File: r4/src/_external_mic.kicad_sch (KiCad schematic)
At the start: 138 parts, among them J27 , Q12 BSS84PW, Q13 BSS84PW, Q14 NX6008NBKW, Q15 NX3008NBKW, Q16 NX3008NBKW, Q17 NX3008NBKW, Q18 NX3008NBKW, Q19 NX3008NBKW, Q20 BSS84PW, Q21 BSS84PW, Q22 NX3008NBKW, Q23 NX3008NBKW, Q24 NX3008NBKW, Q25 BSS84PW, T17 , T18 , T19 , T20 , T21 , T22 , T23 , T24 , T25 , T26 , T27 , T28 , T29 , T30 , T31 , T32 , T33 , T34 , T35 , T36 , T37 , T38 , T43 , T44 , T45 , T46 , T47 , T48 , T49 , T50 , U17 74HC20, U18 THAT5173, U19 74HC74, U20 74HC132, U21 74HC4520, U22 74HC132, U23 THAT1580, U24 74HC688, U25 LM4562, U26 74HC688, U27 AD4005

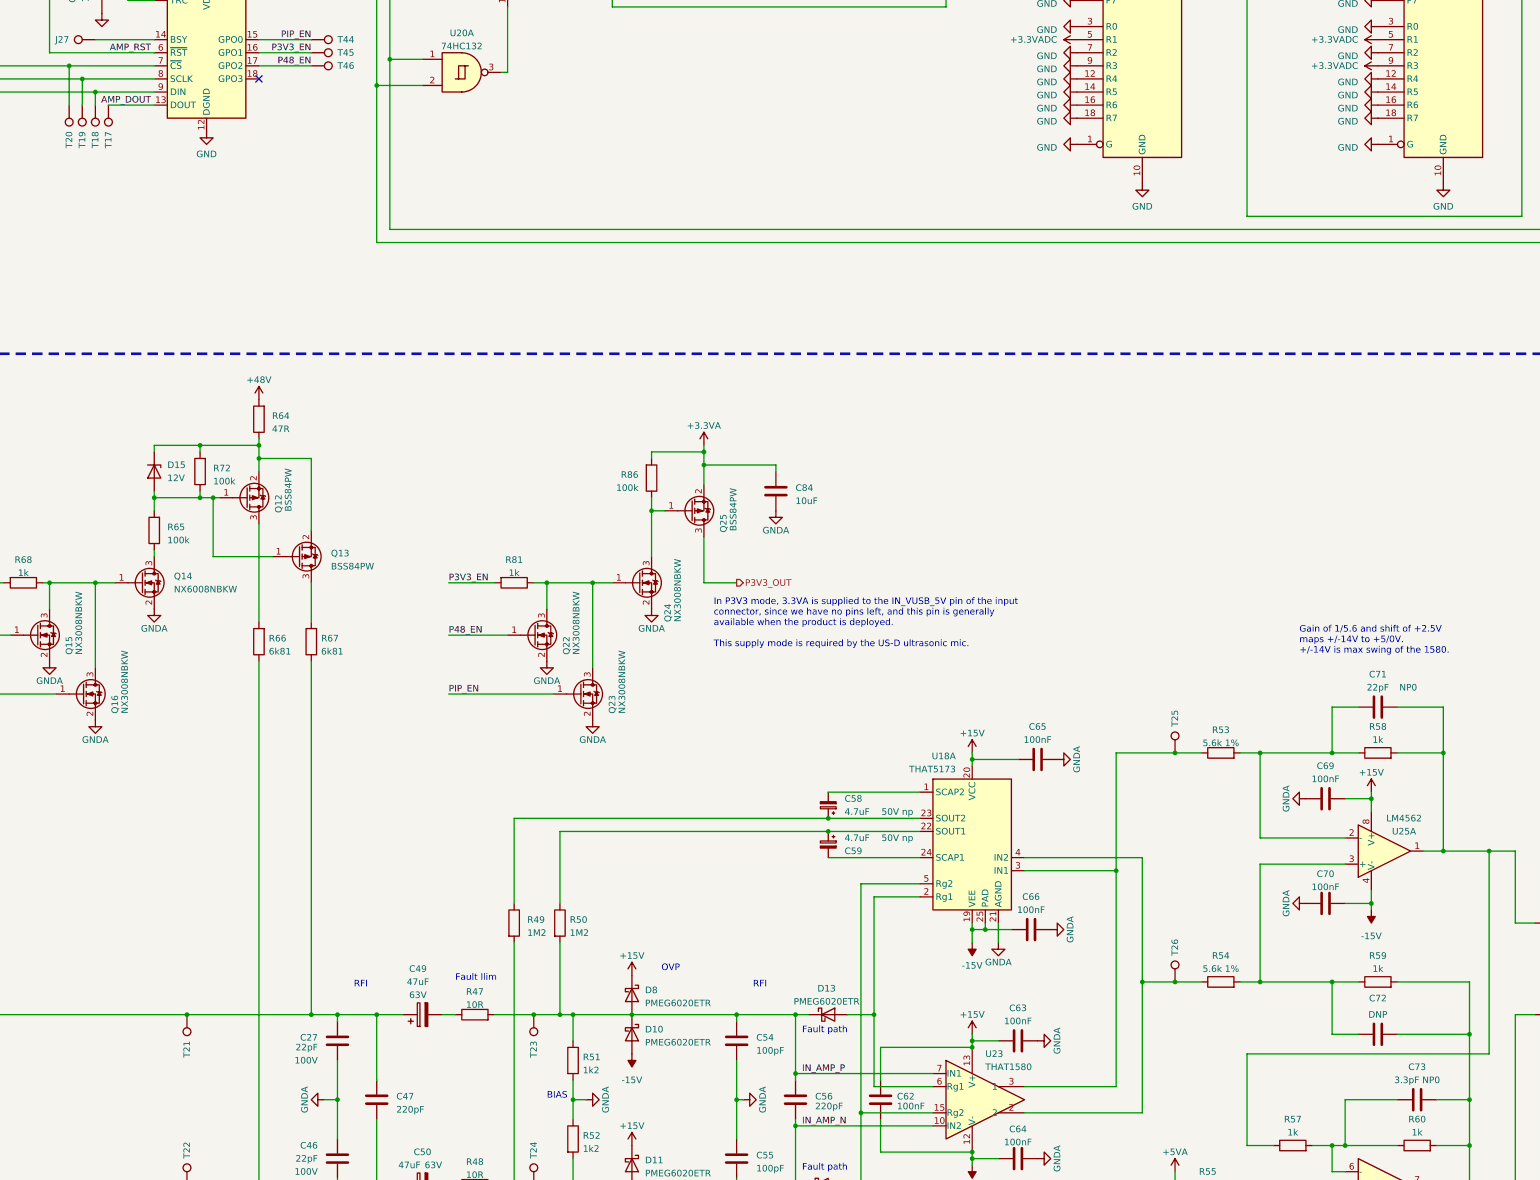
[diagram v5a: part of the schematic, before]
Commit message: Set volage ratings on some caps, change some cap footprints to remove a couple of BOM lines
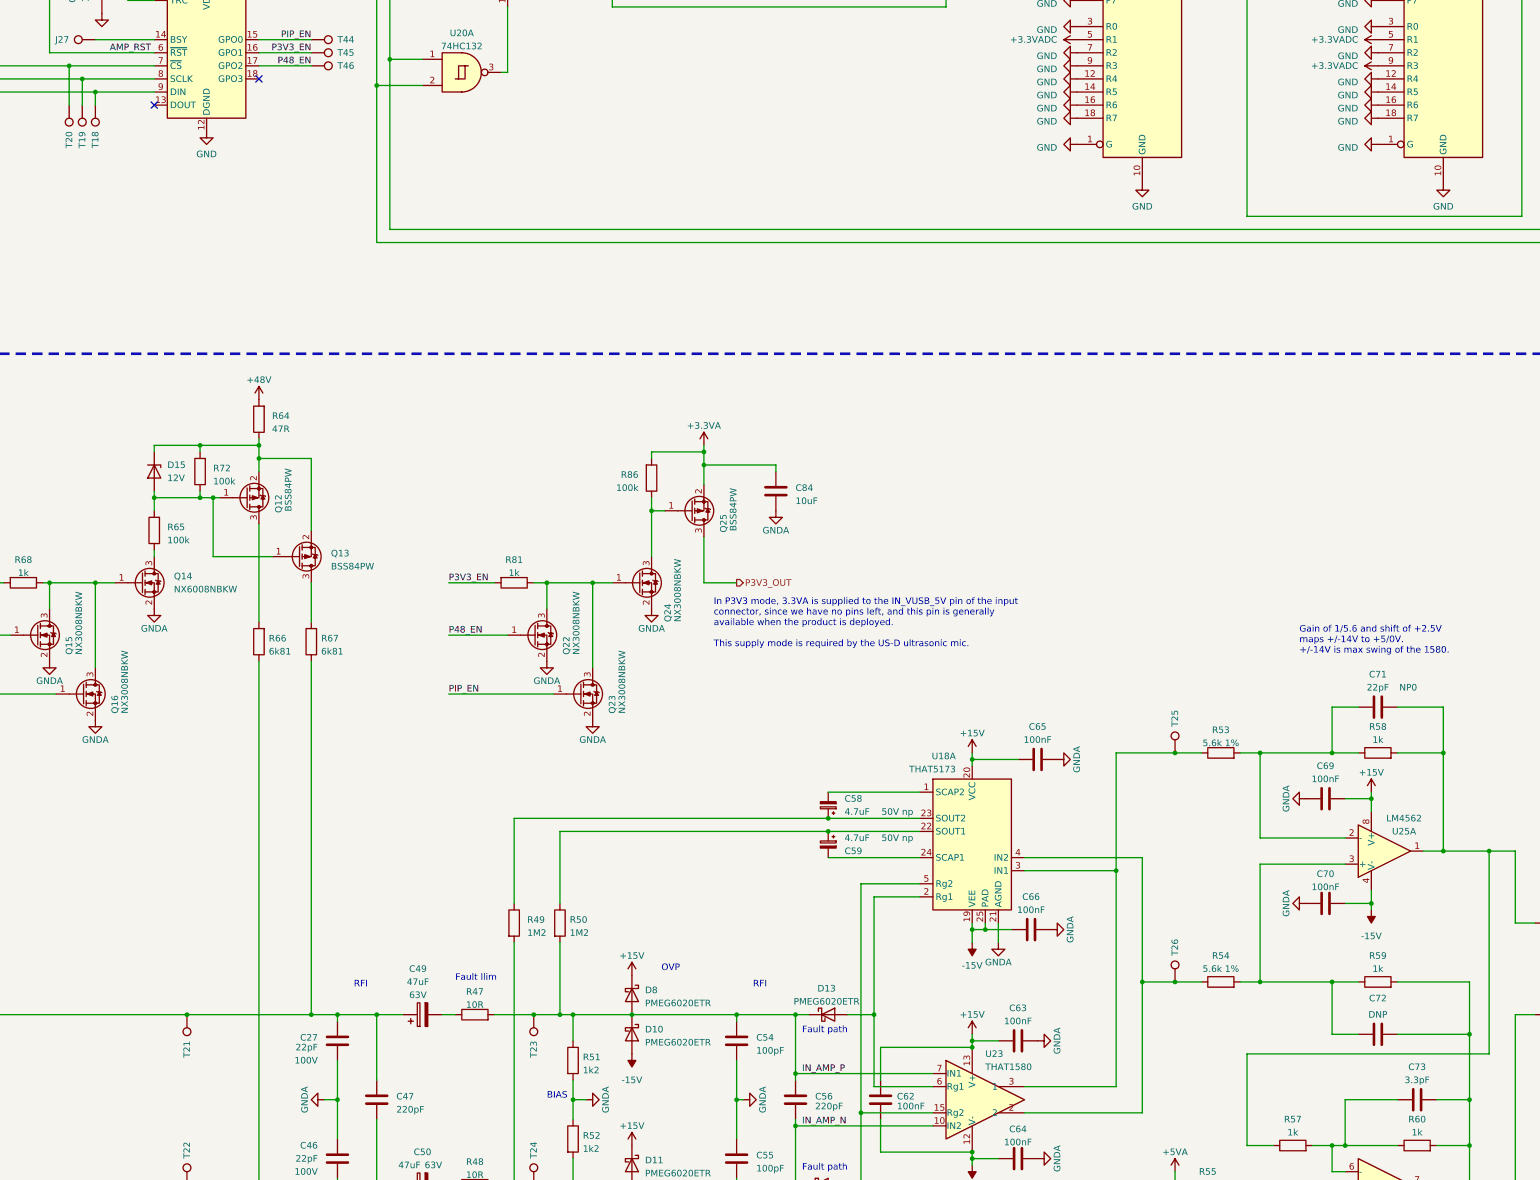
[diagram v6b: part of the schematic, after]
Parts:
- removed T17: (no value), TestPoint:TestPoint_Pad_D1.0mm, symbol Connector:TestPoint
- C56: footprint Capacitor_SMD:C_0201_0603Metric -> Capacitor_SMD:C_0402_1005Metric
- C73: value 3.3pF NP0 -> 3.3pF; Tempco (none) -> NP0
- C77: footprint Capacitor_SMD:C_0805_2012Metric -> Capacitor_SMD:C_0603_1608Metric; Voltage (none) -> 6.3V
- C83, C84: Voltage (none) -> 6.3V
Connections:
- net AMP_DOUT: no longer names the net of U18.13 (DOUT)
- no-connect marks 8 -> 9
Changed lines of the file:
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@@
   (no_connect (at 257.81 118.11))
   (no_connect (at 210.82 31.75))
+  (no_connect (at 181.61 142.24))
   (wire (pts (xy 417.83 276.86) (xy 417.83 275.59))
     (stroke (width 0) (type default))
@@
     (stroke (width 0) (type default))
   )
-  (wire (pts (xy 172.72 142.24) (xy 181.61 142.24))
-    (stroke (width 0) (type default))
-  )
   (wire (pts (xy 482.6 152.4) (xy 482.6 143.51))
     (stroke (width 0) (type default))
@@
     (effects (font (size 1.27 1.27)) (justify left bottom))
   )
-  (label "AMP_DOUT" (at 180.975 142.24 180) (fields_autoplaced)
-    (effects (font (size 1.27 1.27)) (justify right bottom))
-  )
   (label "IN_AMP_P" (at 307.34 330.2 0) (fields_autoplaced)
     (effects (font (size 1.27 1.27)) (justify left bottom))
@@
       (effects (font (size 1.27 1.27)))
     )
-    (property "Value" "3.3pF NP0" (at 426.72 331.47 90)
+    (property "Value" "3.3pF" (at 426.72 331.47 90)
       (effects (font (size 1.27 1.27)))
     )
@@
       (effects (font (size 1.27 1.27)) hide)
     )
+    (property "Tempco" "NP0" (at 426.72 335.28 90)
+      (effects (font (size 1.27 1.27)) hide)
+    )
     (pin "1")
     (pin "2")
@@
       (project "bugg-main-r4"
         (path "/e3eb514f-6ce4-4abe-ba20-f82f0015628f/41f15edd-4583-4f5d-8a81-daeb7c83b416"
-          (reference "C73") (unit 1) (value "3.3pF NP0") (footprint "Capacitor_SMD:C_0402_1005Metric")
+          (reference "C73") (unit 1) (value "3.3pF") (footprint "Capacitor_SMD:C_0402_1005Metric")
         )
       )
@@
       (effects (font (size 1.27 1.27)) hide)
     )
+    (property "Voltage" "6.3V" (at 302.26 217.17 0)
+      (effects (font (size 1.27 1.27)) hide)
+    )
     (pin "1")
     (pin "2")
@@
       (effects (font (size 1.27 1.27)) hide)
     )
+    (property "Voltage" "6.3V" (at 132.08 217.17 0)
+      (effects (font (size 1.27 1.27)) hide)
+    )
     (pin "1")
     (pin "2")
@@
       (effects (font (size 1.27 1.27)) (justify right))
     )
-    (property "Footprint" "Capacitor_SMD:C_0201_0603Metric" (at 305.1048 331.47 0)
+    (property "Footprint" "Capacitor_SMD:C_0402_1005Metric" (at 305.1048 331.47 0)
       (effects (font (size 1.27 1.27)) hide)
     )
@@
       (project "bugg-main-r4"
         (path "/e3eb514f-6ce4-4abe-ba20-f82f0015628f/41f15edd-4583-4f5d-8a81-daeb7c83b416"
-          (reference "C56") (unit 1) (value "220pF") (footprint "Capacitor_SMD:C_0201_0603Metric")
+          (reference "C56") (unit 1) (value "220pF") (footprint "Capacitor_SMD:C_0402_1005Metric")
         )
       )
@@
     )
   )
-  (symbol (lib_id "Connector:TestPoint") (at 172.72 142.24 180) (unit 1)
-    (in_bom yes) (on_board yes) (dnp no)
-    (property "Reference" "T17" (at 172.72 147.32 90)
-      (effects (font (size 1.27 1.27)) (justify left))
-    )
-    (property "Value" " " (at 171.45 147.32 90)
-      (effects (font (size 1.27 1.27)) (justify left))
-    )
-    (property "Footprint" "TestPoint:TestPoint_Pad_D1.0mm" (at 167.64 142.24 0)
-      (effects (font (size 1.27 1.27)) hide)
-    )
-    (property "Datasheet" "~" (at 167.64 142.24 0)
-      (effects (font (size 1.27 1.27)) hide)
-    )
-    (pin "1")
-    (instances
-      (project "bugg-main-r4"
-        (path "/e3eb514f-6ce4-4abe-ba20-f82f0015628f/41f15edd-4583-4f5d-8a81-daeb7c83b416"
-          (reference "T17") (unit 1) (value " ") (footprint "TestPoint:TestPoint_Pad_D1.0mm")
-        )
-      )
-    )
-  )
   (symbol (lib_id "Device:R") (at 76.2 234.95 270) (unit 1)
     (in_bom yes) (on_board yes) (dnp no) (fields_autoplaced)
@@
       (effects (font (size 1.27 1.27)))
     )
-    (property "Footprint" "Capacitor_SMD:C_0805_2012Metric" (at 474.98 276.5552 0)
+    (property "Footprint" "Capacitor_SMD:C_0603_1608Metric" (at 474.98 276.5552 0)
       (effects (font (size 1.27 1.27)) hide)
     )
@@
       (effects (font (size 1.27 1.27)) hide)
     )
+    (property "Voltage" "6.3V" (at 478.79 275.59 90)
+      (effects (font (size 1.27 1.27)) hide)
+    )
     (pin "1")
     (pin "2")
@@
       (project "bugg-main-r4"
         (path "/e3eb514f-6ce4-4abe-ba20-f82f0015628f/41f15edd-4583-4f5d-8a81-daeb7c83b416"
-          (reference "C77") (unit 1) (value "10uF") (footprint "Capacitor_SMD:C_0805_2012Metric")
+          (reference "C77") (unit 1) (value "10uF") (footprint "Capacitor_SMD:C_0603_1608Metric")
         )
       )

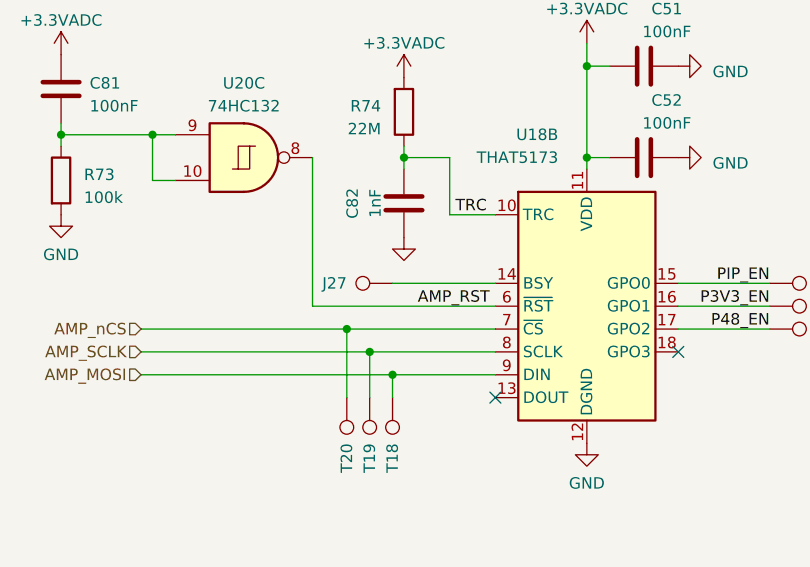
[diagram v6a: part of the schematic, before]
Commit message: Remove unnecessary BSY testpoint
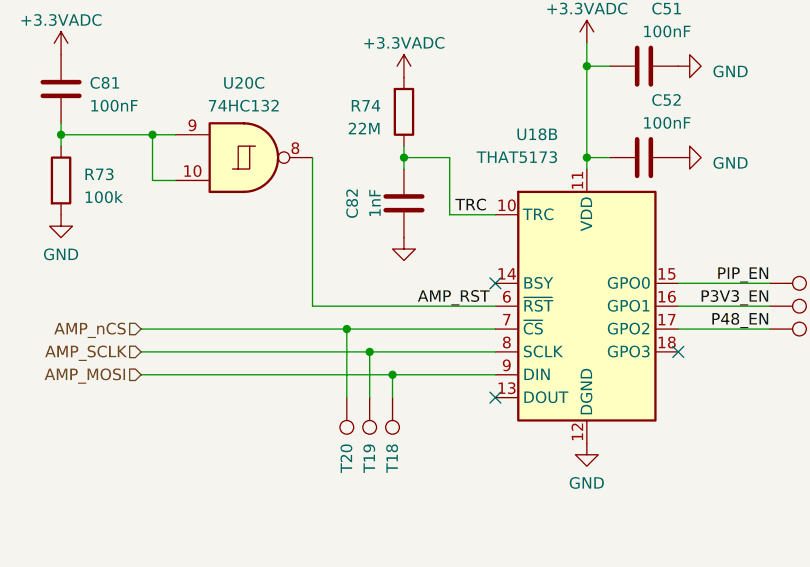
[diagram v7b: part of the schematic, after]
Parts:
- removed J27: (no value), TestPoint:TestPoint_Pad_D1.0mm, symbol Connector:TestPoint
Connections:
- no-connect marks 9 -> 10
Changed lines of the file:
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@@
   (no_connect (at 509.27 119.38))
   (no_connect (at 201.93 137.16))
+  (no_connect (at 181.61 129.54))
   (no_connect (at 257.81 118.11))
   (no_connect (at 210.82 31.75))
@@
     (stroke (width 0) (type default))
   )
-  (wire (pts (xy 181.61 129.54) (xy 170.18 129.54))
-    (stroke (width 0) (type default))
-  )
   (wire (pts (xy 472.44 275.59) (xy 472.44 289.56))
     (stroke (width 0) (type default))
@@
         )
       )
-    )
-  )
-  (symbol (lib_id "Connector:TestPoint") (at 170.18 129.54 90) (unit 1)
-    (in_bom yes) (on_board yes) (dnp no)
-    (property "Reference" "J27" (at 165.1 129.54 90)
-      (effects (font (size 1.27 1.27)) (justify left))
-    )
-    (property "Value" " " (at 165.1 128.27 90)
-      (effects (font (size 1.27 1.27)) (justify left))
-    )
-    (property "Footprint" "TestPoint:TestPoint_Pad_D1.0mm" (at 170.18 124.46 0)
-      (effects (font (size 1.27 1.27)) hide)
-    )
-    (property "Datasheet" "~" (at 170.18 124.46 0)
-      (effects (font (size 1.27 1.27)) hide)
-    )
-    (pin "1")
-    (instances
-      (project "bugg-main-r4"
-        (path "/e3eb514f-6ce4-4abe-ba20-f82f0015628f/41f15edd-4583-4f5d-8a81-daeb7c83b416"
-          (reference "J27") (unit 1) (value " ") (footprint "TestPoint:TestPoint_Pad_D1.0mm")
-        )
-      )

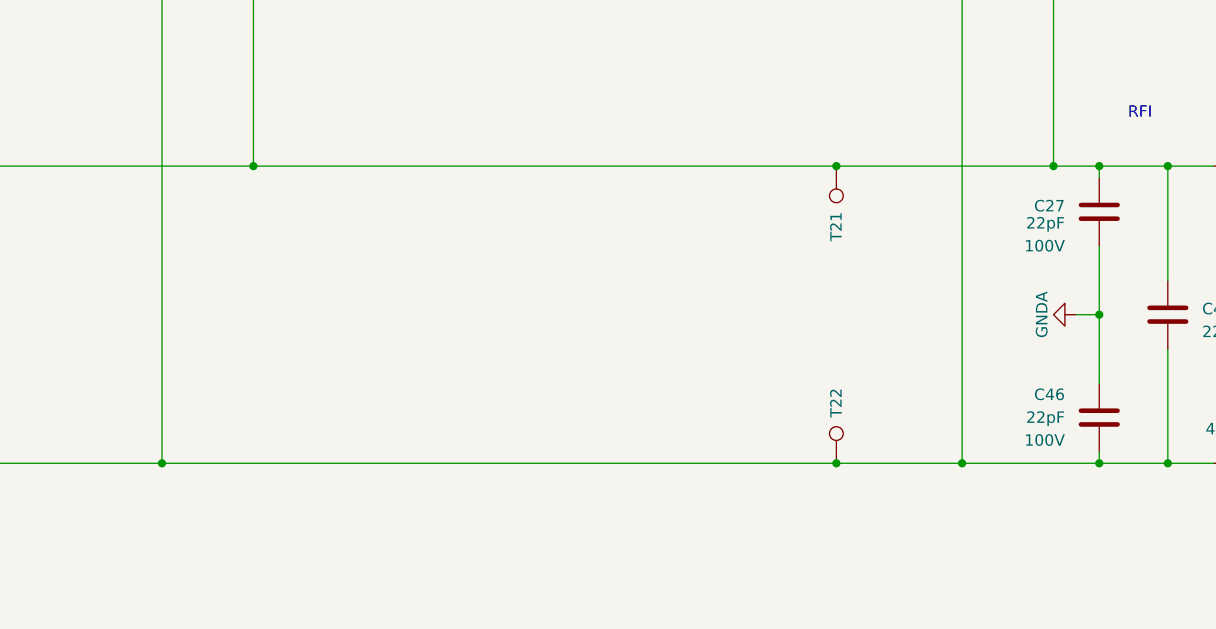
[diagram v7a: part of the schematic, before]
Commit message: Remove testpoints from mic inputs - there's no space for them
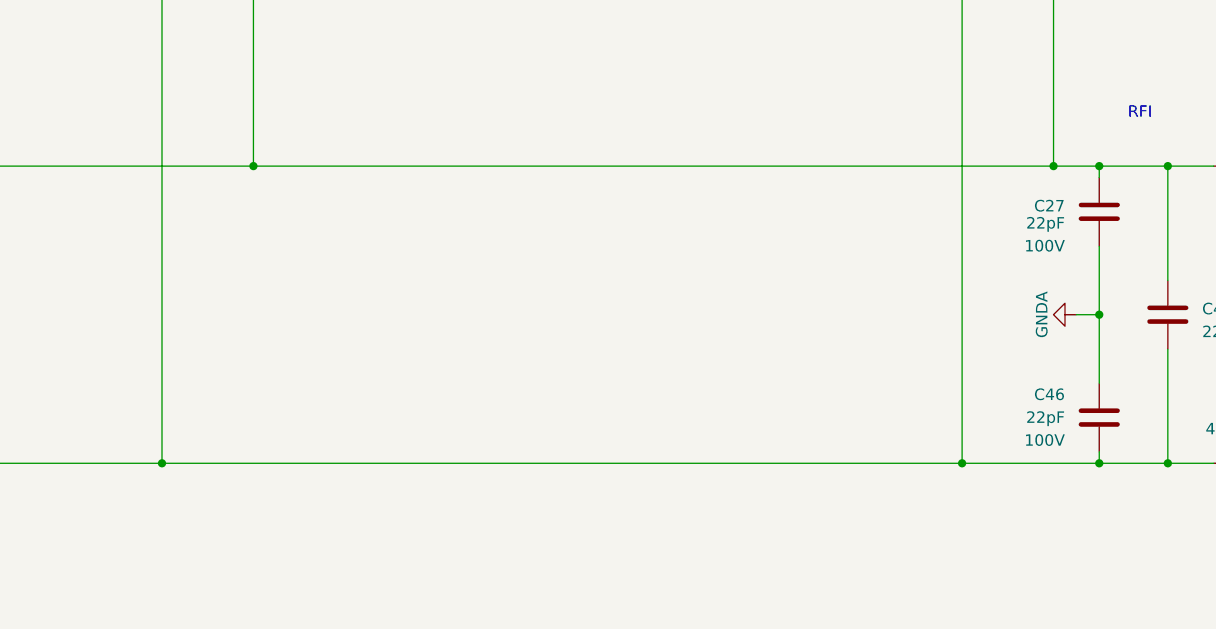
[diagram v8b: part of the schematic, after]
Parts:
- removed T21, T22: (no value), TestPoint:TestPoint_Pad_D1.0mm, symbol Connector:TestPoint
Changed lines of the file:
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@@
   (junction (at 340.36 302.26) (diameter 0) (color 0 0 0 0)
   )
-  (junction (at 187.96 318.77) (diameter 0) (color 0 0 0 0)
-  )
   (junction (at 262.89 351.79) (diameter 0) (color 0 0 0 0)
   )
@@
   (junction (at 528.32 143.51) (diameter 0) (color 0 0 0 0)
   )
-  (junction (at 187.96 351.79) (diameter 0) (color 0 0 0 0)
-  )
   (junction (at 306.07 82.55) (diameter 0) (color 0 0 0 0)
   )
@@
     (stroke (width 0) (type default))
   )
-  (wire (pts (xy 187.96 351.79) (xy 201.93 351.79))
+  (wire (pts (xy 113.03 351.79) (xy 201.93 351.79))
     (stroke (width 0) (type default))
   )
@@
     (stroke (width 0) (type default))
   )
-  (wire (pts (xy 123.19 318.77) (xy 187.96 318.77))
-    (stroke (width 0) (type default))
-  )
   (wire (pts (xy 142.24 137.16) (xy 167.64 137.16))
     (stroke (width 0) (type default))
@@
     (stroke (width 0) (type default))
   )
-  (wire (pts (xy 187.96 318.77) (xy 212.09 318.77))
+  (wire (pts (xy 123.19 318.77) (xy 212.09 318.77))
     (stroke (width 0) (type default))
   )
@@
     (stroke (width 0) (type default))
   )
-  (wire (pts (xy 113.03 351.79) (xy 187.96 351.79))
-    (stroke (width 0) (type default))
-  )
   (wire (pts (xy 33.02 31.75) (xy 33.02 21.59))
     (stroke (width 0) (type default))
@@
     )
   )
-  (symbol (lib_id "Connector:TestPoint") (at 187.96 318.77 0) (mirror x) (unit 1)
-    (in_bom yes) (on_board yes) (dnp no)
-    (property "Reference" "T21" (at 187.96 323.85 90)
-      (effects (font (size 1.27 1.27)) (justify left))
-    )
-    (property "Value" " " (at 189.23 323.85 90)
-      (effects (font (size 1.27 1.27)) (justify left))
-    )
-    (property "Footprint" "TestPoint:TestPoint_Pad_D1.0mm" (at 193.04 318.77 0)
-      (effects (font (size 1.27 1.27)) hide)
-    )
-    (property "Datasheet" "~" (at 193.04 318.77 0)
-      (effects (font (size 1.27 1.27)) hide)
-    )
-    (pin "1")
-    (instances
-      (project "bugg-main-r4"
-        (path "/e3eb514f-6ce4-4abe-ba20-f82f0015628f/41f15edd-4583-4f5d-8a81-daeb7c83b416"
-          (reference "T21") (unit 1) (value " ") (footprint "TestPoint:TestPoint_Pad_D1.0mm")
-        )
-      )
-    )
-  )
   (symbol (lib_id "power:+3.3VA") (at 113.03 208.28 0) (unit 1)
     (in_bom yes) (on_board yes) (dnp no) (fields_autoplaced)
@@
         )
       )
-    )
-  )
-  (symbol (lib_id "Connector:TestPoint") (at 187.96 351.79 0) (mirror y) (unit 1)
-    (in_bom yes) (on_board yes) (dnp no)
-    (property "Reference" "T22" (at 187.96 346.71 90)
-      (effects (font (size 1.27 1.27)) (justify left))
-    )
-    (property "Value" " " (at 186.69 346.71 90)
-      (effects (font (size 1.27 1.27)) (justify left))
-    )
-    (property "Footprint" "TestPoint:TestPoint_Pad_D1.0mm" (at 182.88 351.79 0)
-      (effects (font (size 1.27 1.27)) hide)
-    )
-    (property "Datasheet" "~" (at 182.88 351.79 0)
-      (effects (font (size 1.27 1.27)) hide)
-    )
-    (pin "1")
-    (instances
-      (project "bugg-main-r4"
-        (path "/e3eb514f-6ce4-4abe-ba20-f82f0015628f/41f15edd-4583-4f5d-8a81-daeb7c83b416"
-          (reference "T22") (unit 1) (value " ") (footprint "TestPoint:TestPoint_Pad_D1.0mm")
-        )
-      )
